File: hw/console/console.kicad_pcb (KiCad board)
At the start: 2 copper layers, 156 x 74 mm, 148 parts, among them J1 Batt, J301 USB-C 16P, J501 SPK 8R, J601 FFC-40 0.5mm, J901 UART, Q601 AO3400A, SW1 Движок, SW101 UP, SW102 DOWN, SW103 LEFT, SW104 RIGHT, SW105 SELECT, SW106 START, SW107 A, SW108 B, SW109 C, SW110 D, U1 F133-A, U2 SY8089AAAC, U3 SY8089AAAC, U4 SY8089AAAC, U401 W25Q32JVSSIQ, U5 TP4056, U501 PAM8301, Y1 24 МГц, Y2 32.768 кГц

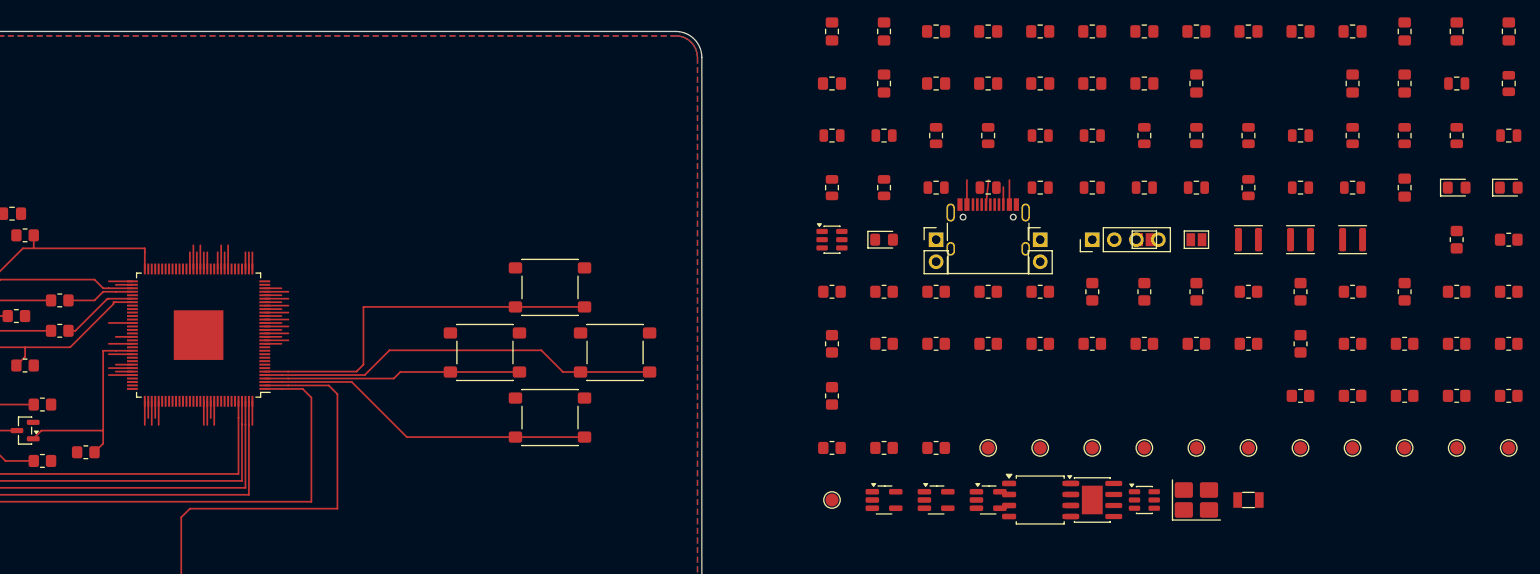
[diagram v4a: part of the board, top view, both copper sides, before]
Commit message: hw: такт, сброс и развязка вокруг чипа
Кварцы стоят вертикально — тогда обе линии идут от чипа прямо, без
обхода корпуса кругом. Сброс поднимается вплотную к боку: прямо ему
идти некуда, там кварц. Всё по лицу, переходных нет, DRC чистый.

Кольцо развязки перестало ходить рядами вдоль стороны и ищет ближайшее
свободное место от своего вывода. Рядами место выбиралось по интервалу
ВДОЛЬ бока — пока бока были пусты, это совпадало с «близко», а теперь
левый занят разъёмом шлейфа. Средняя 12.7 -> 9.6 мм, худшая 32.2 ->
18.2, девять ёмкостей перестали лежать внахлёст.

Требование блока 8 «не дальше 3.5 мм» по-прежнему не выполнено, и это
записано числом в 08-decoupling.md §6.7.1, а не замолчано.

Кольцо теперь знает про полосы ручной разводки: оно читает таблицу
pcb_hand.ROUTES, а не медь платы, потому что медь снимает веер.

Co-Authored-By: Claude Opus 5 (1M context) <noreply@anthropic.com>
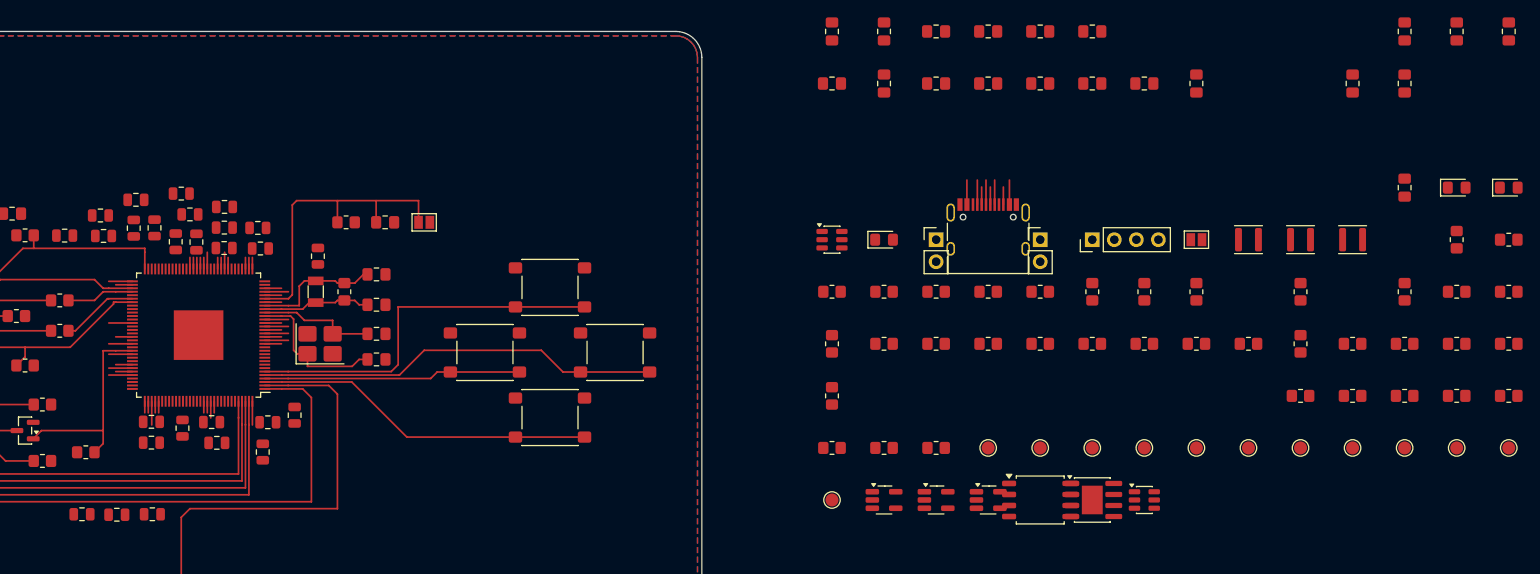
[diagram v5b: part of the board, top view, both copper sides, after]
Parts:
- moved C816 156.5 mm to (146.1, 85.7), turned to 90 degrees
- moved C815 152.8 mm to (140.5, 62.7)
- moved C801 152.8 mm to (140.8, 59.4)
- moved C802 152.3 mm to (147.8, 64.3)
- moved C827 143.4 mm to (142.7, 95.6)
- moved C814 142.2 mm to (145.4, 64.2)
- moved C826 141.5 mm to (138.6, 95.7)
- moved C812 138.4 mm to (137.0, 63.6)
- moved C824 130.6 mm to (132.6, 63.5)
- moved C823 128.1 mm to (134.6, 95.6)
- moved C813 126.1 mm to (159.1, 84.2)
- moved C810 120.5 mm to (142.9, 62.6)
- moved C811 118.3 mm to (151.0, 60.2), turned to 0 degrees
- moved C825 117.6 mm to (155.4, 88.5)
- moved R20 116.2 mm to (164.8, 70.0), turned to 90 degrees
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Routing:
- net RESET: track 2.72 -> 36.0 mm
- net DXOUT: track 1.93 -> 17.5 mm
- net X32KIN: track 2.72 -> 14.9 mm
- net DXIN: track 2.72 -> 13.8 mm
- net X32KOUT: track 1.93 -> 12.5 mm
- net Net-(D301-I/O1-Pad1): track 0.00 -> 4.05 mm
- net +1V8: track 14.0 -> 10.5 mm
- net Net-(J301-CC1): track 0.00 -> 2.82 mm
- net Net-(D301-I/O2-Pad3): track 2.84 -> 5.65 mm
- net +0V9: track 10.4 -> 8.42 mm
- net USB0-DP: track 2.72 -> 1.32 mm
- net USB0-DM: track 2.72 -> 1.32 mm
- net TDI: track 2.72 -> 1.32 mm
- net TCK: track 2.72 -> 1.32 mm
- net GPADC0: track 2.72 -> 1.32 mm
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
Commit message: hw: питание, зарядник, USB и звук расставлены
Три понижающих идут полосой над чипом: на верхней стороне корпуса
сидят выводы 46…51 — питание DRAM и ядра, самые тяжёлые. Полоса
y 40…59 пуста от края до края, поэтому ячейки стоят в ряд, а не
стопкой: стопкой делители налезают на соседний ряд.

Зарядник и батарея — туда же, к движку питания. VSYS общий узел и
несёт весь ток платы, VBUS работает только при зарядке, поэтому
длинной сделана вторая цепь, а не первая.

USB-розетка у нижнего края прямо под выводами 114/115 — пара идёт
вверх коротко. Звук между подъёмами SELECT и START: выходы кодека
тоже на нижней стороне корпуса.

Порядок расстановки в main() теперь блочный и совпадает с порядком
разводки. Прежние bucks/crystals/usb/leds не вызываются: они считали
корпус в другой ориентации и дисплей на параллельной шине.

Перекрытий областей установки ноль, на плате 116 корпусов из 135.

Co-Authored-By: Claude Opus 5 (1M context) <noreply@anthropic.com>
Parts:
- moved D1 240.0 mm to (53.0, 57.0)
- moved D2 237.0 mm to (62.0, 57.0)
- moved R1 213.3 mm to (80.0, 53.0), turned to 0 degrees
- moved C4 209.6 mm to (89.5, 46.0)
- moved R7 201.1 mm to (76.0, 53.0)
- moved U5 194.3 mm to (61.5, 51.0)
- moved R2 191.8 mm to (84.0, 53.0), turned to 0 degrees
- moved C7 188.0 mm to (93.0, 46.0)
- moved L1 184.9 mm to (85.0, 46.0)
- moved C2 181.1 mm to (106.0, 46.0)
- moved J1 180.5 mm to (53.0, 51.0)
- moved C14 180.1 mm to (71.0, 47.0)
- moved R3 177.8 mm to (110.0, 53.0), turned to 0 degrees
- moved R8 177.4 mm to (106.0, 53.0)
- moved C13 177.3 mm to (68.0, 50.0)
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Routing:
- net VBUS: track 5.65 -> 4.85 mm

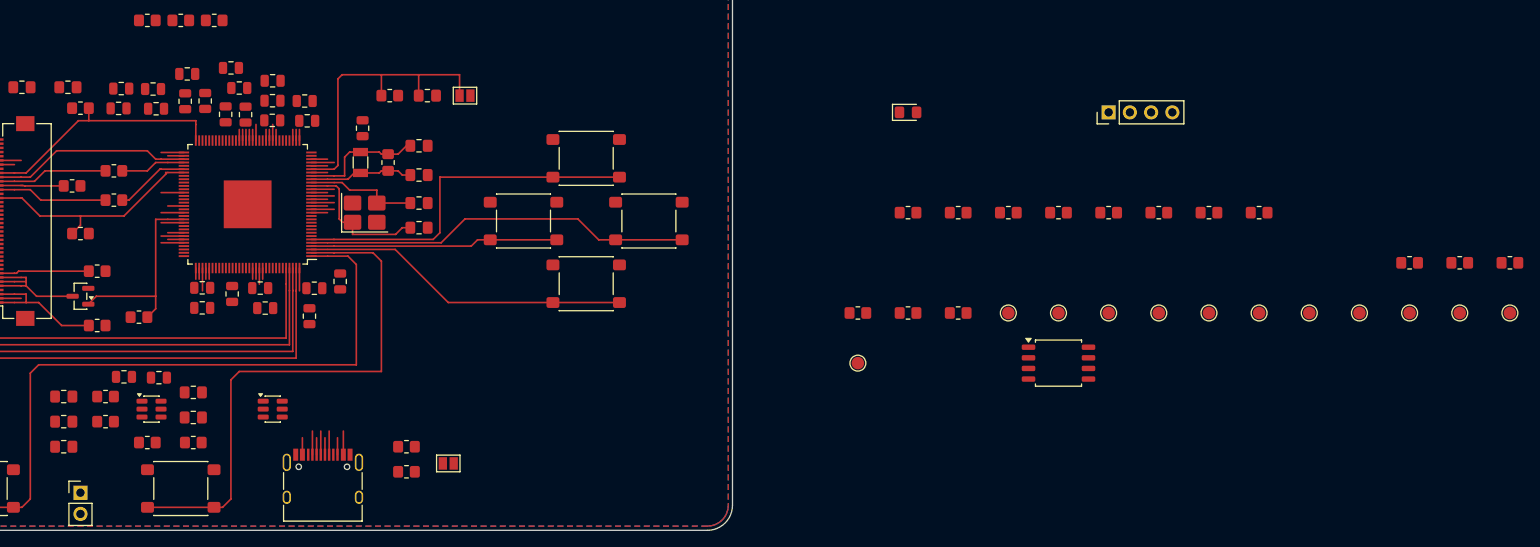
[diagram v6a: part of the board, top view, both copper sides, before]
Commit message: hw: звука в первой ревизии нет — 22 заклёпки стали 6
Полосы крестовины идут поперёк платы на y 91…95 и работают забором:
всё, что приходит с нижнего края, обязано его пересечь, а без
металлизации отверстий каждое пересечение — заклёпка вручную.

Замерено: через забор шли 11 цепей, семь из них звук — усилитель
стоял под забором, кодек над ним. Без звука осталось три (пара USB и
VBUS), то есть шесть заклёпок вместо двадцати двух.

Заодно снята обвязка аналога кодека: слушать его нечем, а место у
корпуса дорогое — четыре из шести худших позиций развязки занимали
как раз C823, C825, C826, C827. Развязка сразу стала 8.3 мм средней
вместо 10.0, дальше 12 мм осталось два конденсатора вместо шести.

Питание AVCC/HPVCC и привязка AGND оставлены: это выводы чипа, а не
наша обвязка, и стоят они двух деталей. ТЗ такой приём разрешает
прямо — «питание необязательных узлов через 0 Ω».

Вернуть звук во второй ревизии стоит одиннадцати деталей усилителя,
трёх конденсаторов кодека и разводки низа платы. Обе таблицы
расстановки и вся схема узла сохранены.

ERC чистый, DRC чистый, перекрытий ноль.

Co-Authored-By: Claude Opus 5 (1M context) <noreply@anthropic.com>
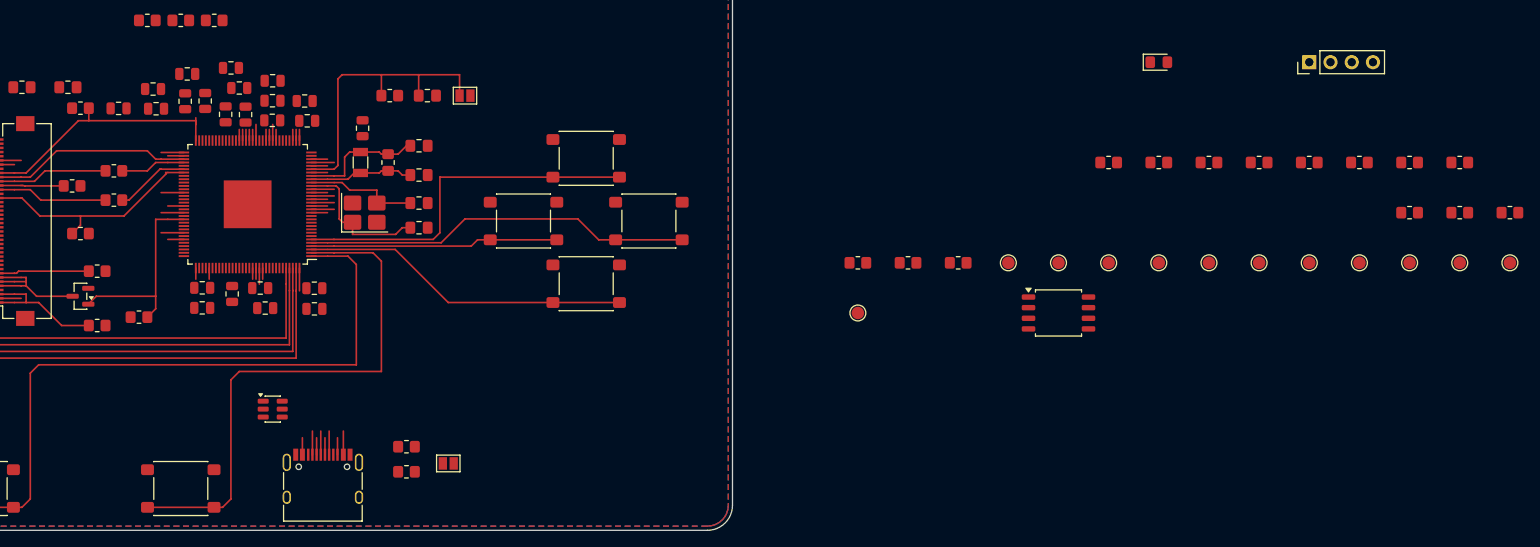
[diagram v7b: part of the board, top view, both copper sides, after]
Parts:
- removed C501, C502, C505: 10u, Capacitor_SMD:C_0805_2012Metric_Pad1.18x1.45mm_HandSolder
- removed C503: 0.1u, Capacitor_SMD:C_0805_2012Metric_Pad1.18x1.45mm_HandSolder
- removed C504: 1u, Capacitor_SMD:C_0805_2012Metric_Pad1.18x1.45mm_HandSolder
- removed C823: 2.2u, Capacitor_SMD:C_0805_2012Metric
- removed C825: 0.1u, Capacitor_SMD:C_0805_2012Metric
- removed C826, C827: 0.47u, Capacitor_SMD:C_0805_2012Metric
- removed J501: SPK 8R, Connector_PinHeader_2.54mm:PinHeader_1x02_P2.54mm_Vertical
- removed R501, R502: 47k, Resistor_SMD:R_0805_2012Metric_Pad1.20x1.40mm_HandSolder
- removed R503: 0, Resistor_SMD:R_0805_2012Metric_Pad1.20x1.40mm_HandSolder
- removed R504: 10k, Resistor_SMD:R_0805_2012Metric_Pad1.20x1.40mm_HandSolder
- removed U501: PAM8301, Package_TO_SOT_SMD:SOT-23-6
- moved D901 30.6 mm to (257.0, 58.0)
- moved J901 24.7 mm to (275.0, 58.0)
- moved R401 24.7 mm to (251.0, 70.0)
- moved R402 24.7 mm to (257.0, 70.0)
- moved R403 24.7 mm to (263.0, 70.0)
- moved R404 24.7 mm to (269.0, 70.0)
- moved R408 24.7 mm to (275.0, 70.0)
- moved R409 24.7 mm to (281.0, 70.0)
- moved R410 24.7 mm to (287.0, 70.0)
- moved R411 24.7 mm to (293.0, 70.0)
- moved R801 6.00 mm to (287.0, 76.0)
- moved R802 6.00 mm to (293.0, 76.0)
- moved R803 6.00 mm to (299.0, 76.0)
- moved R804 6.00 mm to (221.0, 82.0)
- moved R9 6.00 mm to (227.0, 82.0)
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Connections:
- U1 pad 100: HPOUTFB -> unconnected-(U1-HPOUTFB-Pad100)
- U1 pad 86: AMP-SD -> unconnected-(U1-PB2-Pad86)
- U1 pad 90: VRA2 -> unconnected-(U1-VRA2-Pad90)
- U1 pad 92: VRA1 -> unconnected-(U1-VRA1-Pad92)
- U1 pad 98: HPOUTR -> unconnected-(U1-HPOUTR-Pad98)
- U1 pad 99: HPOUTL -> unconnected-(U1-HPOUTL-Pad99)
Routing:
- net VRA2: track 2.72 -> 0.00 mm
- net VRA1: track 2.72 -> 0.00 mm
- net HPOUTL: track 2.72 -> 0.00 mm
- net AMP-SD: track 2.72 -> 0.00 mm
- net HPOUTR: track 1.33 -> 0.00 mm
- net HPOUTFB: track 1.33 -> 0.00 mm
- net AVCC: track 3.25 -> 4.05 mm
- net LCD-CS: track 30.1 -> 30.9 mm

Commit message: hw: расставлено всё, кроме флешки
Нашлись детали, которых не ставила ни одна функция расстановки:
перемычки питания VCC-TVOUT и AVCC, резистор DZQ, привязка AGND,
контрольные точки такта и рельс, хвосты ячейки +0V9. Они ездили
за краем платы, пока всё остальное стояло, и вылезли только на
подсчёте стоянки. Обвязка F133 теперь ставится тем же поиском
ближайшего места, что и развязка.

Отладка — в верхнюю полосу: все шесть её сигналов выходят с верхней
стороны корпуса. Разъём UART лёжа у верхнего края: у гребёнки начало
координат на первом выводе, и стоя она тянулась на девять миллиметров
вниз, прямо на точки JTAG.

На стоянке — только флешка, 10 деталей. Перекрытий ноль.

Co-Authored-By: Claude Opus 5.5 <noreply@anthropic.com>
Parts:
- moved TP5 182.7 mm to (82.0, 57.5)
- moved TP4 180.7 mm to (78.0, 57.5)
- moved R9 177.1 mm to (54.0, 44.0)
- moved R801 155.3 mm to (132.4, 61.1)
- moved R802 144.1 mm to (150.0, 57.9)
- moved TP1 143.1 mm to (100.5, 46.0)
- moved R803 140.2 mm to (159.1, 84.3), turned to 90 degrees
- moved TP802 136.3 mm to (138.9, 88.9)
- moved TP904 129.2 mm to (172.5, 55.5)
- moved TP903 126.8 mm to (169.0, 55.5)
- moved TP902 124.4 mm to (165.5, 55.5)
- moved TP901 121.9 mm to (162.0, 55.5)
- moved TP2 120.0 mm to (130.5, 46.0)
- moved J901 113.1 mm to (163.0, 42.5)
- moved TP801 105.6 mm to (164.6, 66.5)
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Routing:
- net KEY-LEFT: track 130.1 -> 0.00 mm
- net KEY-UP: track 115.6 -> 0.00 mm
- net KEY-DOWN: track 104.6 -> 0.00 mm
- net KEY-RIGHT: track 103.2 -> 0.00 mm
- net KEY-SELECT: track 82.6 -> 0.00 mm
- net KEY-START: track 65.1 -> 0.00 mm
- net KEY-A: track 46.5 -> 0.00 mm
- net KEY-D: track 43.9 -> 0.00 mm
- net KEY-C: track 39.4 -> 0.00 mm
- net RESET: track 36.0 -> 0.00 mm
- net LCD-CS: track 30.9 -> 0.00 mm
- net KEY-B: track 29.7 -> 0.00 mm
- net LCD-RST: track 27.9 -> 0.00 mm
- net LCD-DC: track 23.9 -> 0.00 mm
- net LCD-BL: track 23.9 -> 0.00 mm
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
